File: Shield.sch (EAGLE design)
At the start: 77 parts

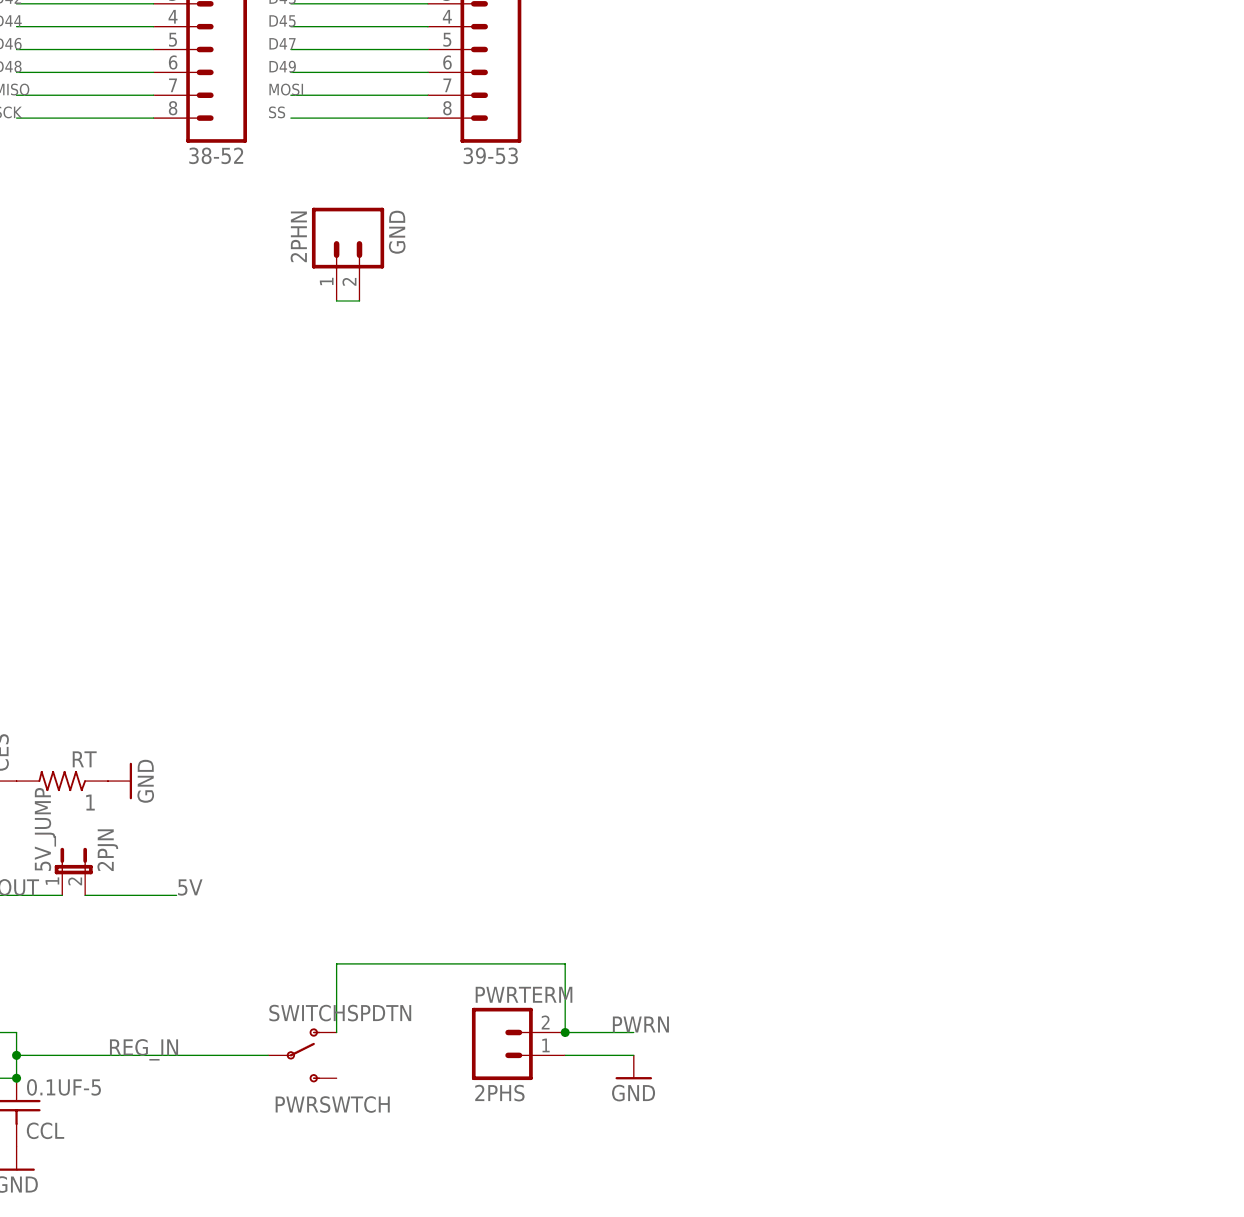
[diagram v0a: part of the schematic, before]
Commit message: Added charging circuit to schematic
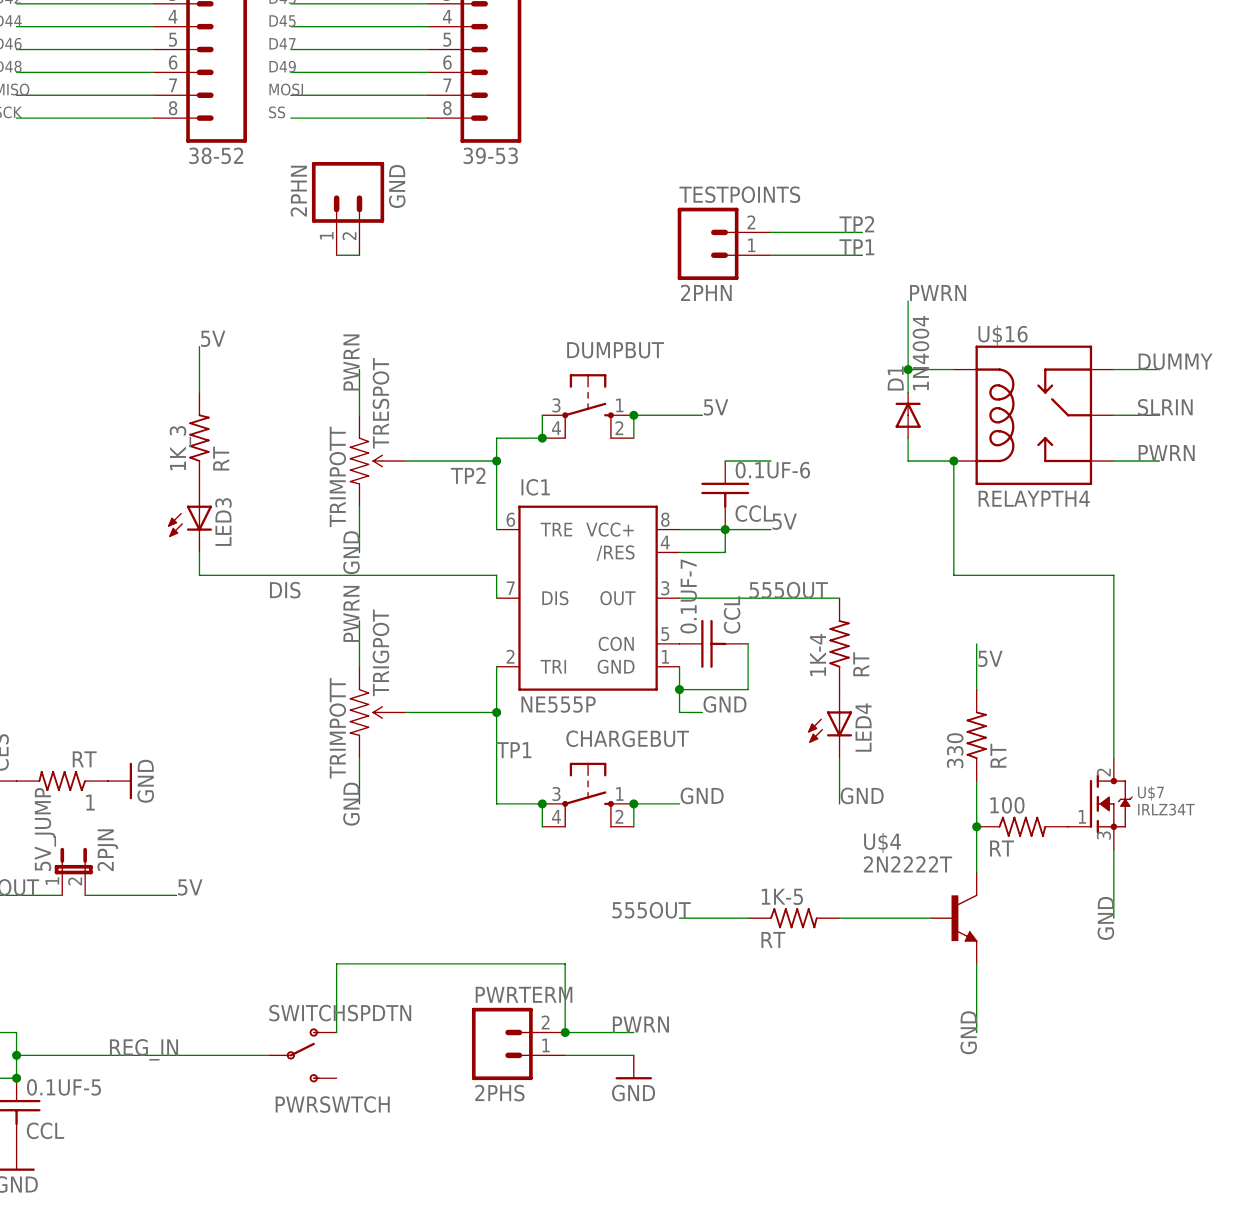
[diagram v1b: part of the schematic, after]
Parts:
- added 0.1UF-6, 0.1UF-7: CCL, LEMS:CCL
- added 100, 1K-4, 1K-5, 1K_3, 330: RT, LEMS:RT
- added CHARGEBUT, DUMPBUT: (no value), LEMS:10-XXN
- added D1: 1N4004, LEMS:1N4004
- added IC1: NE555P, LEMS:NE555P
- added LED3, LED4: (no value), LEMS:LED3MM
- added TESTPOINTS: 2PHN, LEMS:2PHN
- added TRESPOT, TRIGPOT: TRIMPOTT, LEMS:TRIMPOTT
- added U$16: RELAYPTH4, LEMS:RELAYPTH4
- added U$4: 2N2222T, LEMS:2N2222T
- added U$7: IRLZ34T, LEMS:IRLZ34T
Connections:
- new net 555OUT: 1K-4.2, 1K-5.1, IC1.OUT
- new net DIS: IC1.DIS, LED3.C
- new net DUMMY: U$16.NC
- new net N$10: 1K-4.1, LED4.A
- new net N$11: 100.1, 330.1, U$4.C
- new net N$12: 1K-5.2, U$4.B
- new net N$13: 100.2, U$7.G
- new net N$15: D1.A, U$16.COIL2, U$7.D
- new net N$8: 1K_3.1, LED3.A
- new net N$9: 0.1UF-7.1, IC1.CON
- new net SLRIN: U$16.MAIN
- new net TP1: CHARGEBUT.P, CHARGEBUT.P1, IC1.TRI, TESTPOINTS.1, TRIGPOT.WIPER
- new net TP2: DUMPBUT.P, DUMPBUT.P1, IC1.TRE, TESTPOINTS.2, TRESPOT.WIPER
- net 5V: now also 0.1UF-6.2, 1K_3.2, 330.2, DUMPBUT.S, DUMPBUT.S1, IC1./RES, IC1.VCC+
- net GND: now also 0.1UF-6.1, 0.1UF-7.2, CHARGEBUT.S, CHARGEBUT.S1, IC1.GND, LED4.C, TRESPOT.CW, TRIGPOT.CW, U$4.E, U$7.S
- net PWRN: now also D1.C, TRESPOT.CCW, TRIGPOT.CCW, U$16.COIL1, U$16.NO
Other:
- moved on the sheet: GND

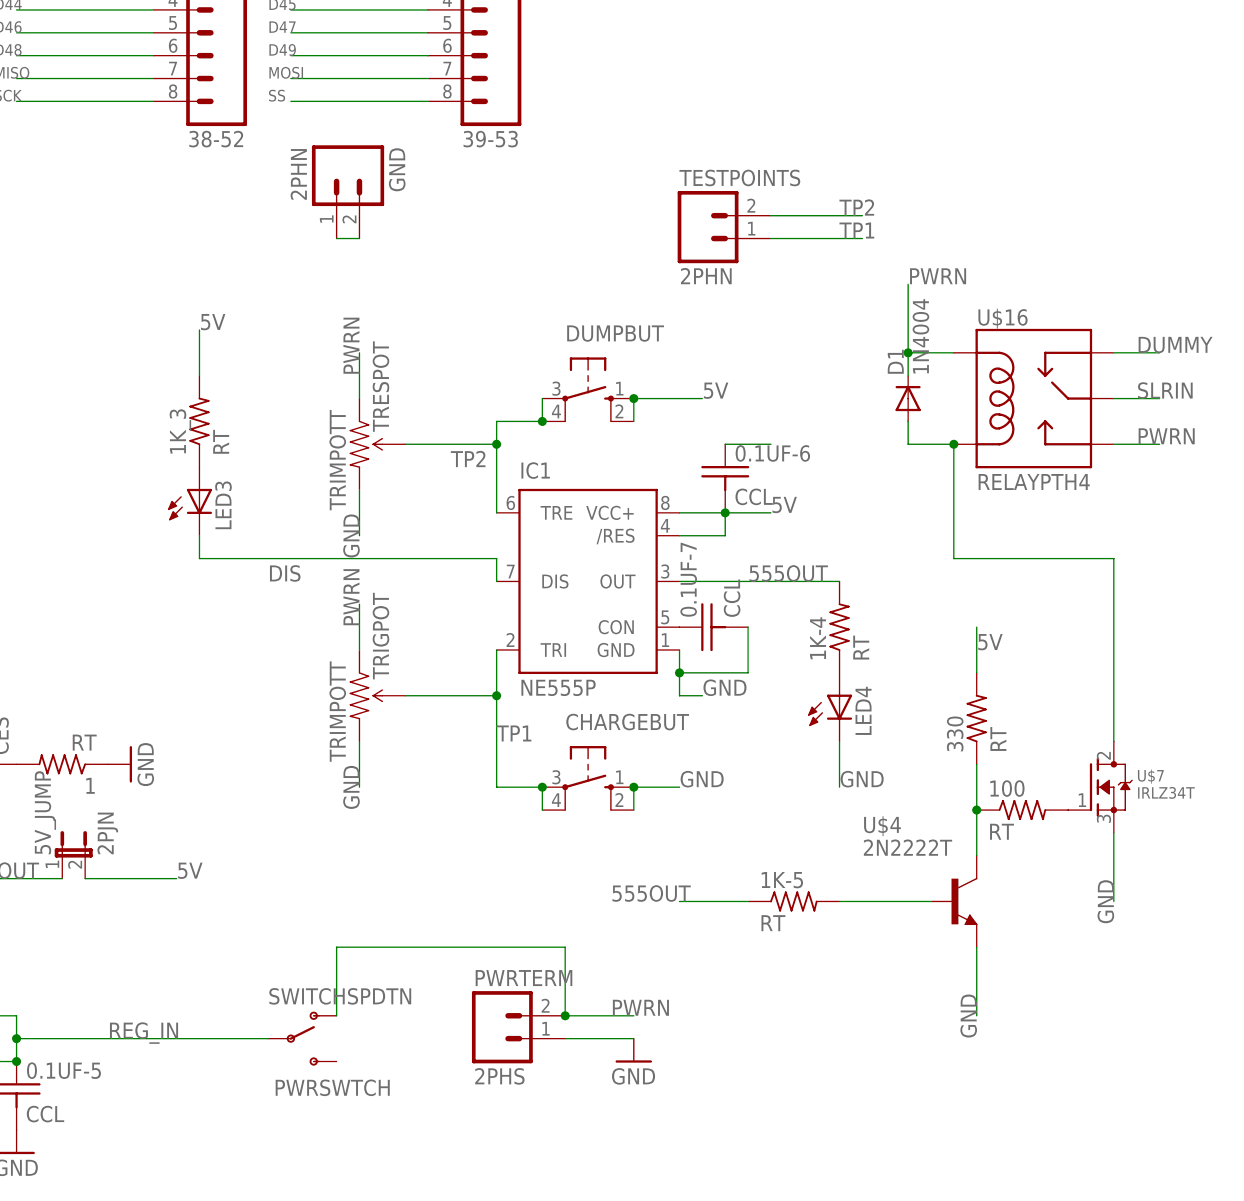
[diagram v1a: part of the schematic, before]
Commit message: Changed charging circuit, finished routing
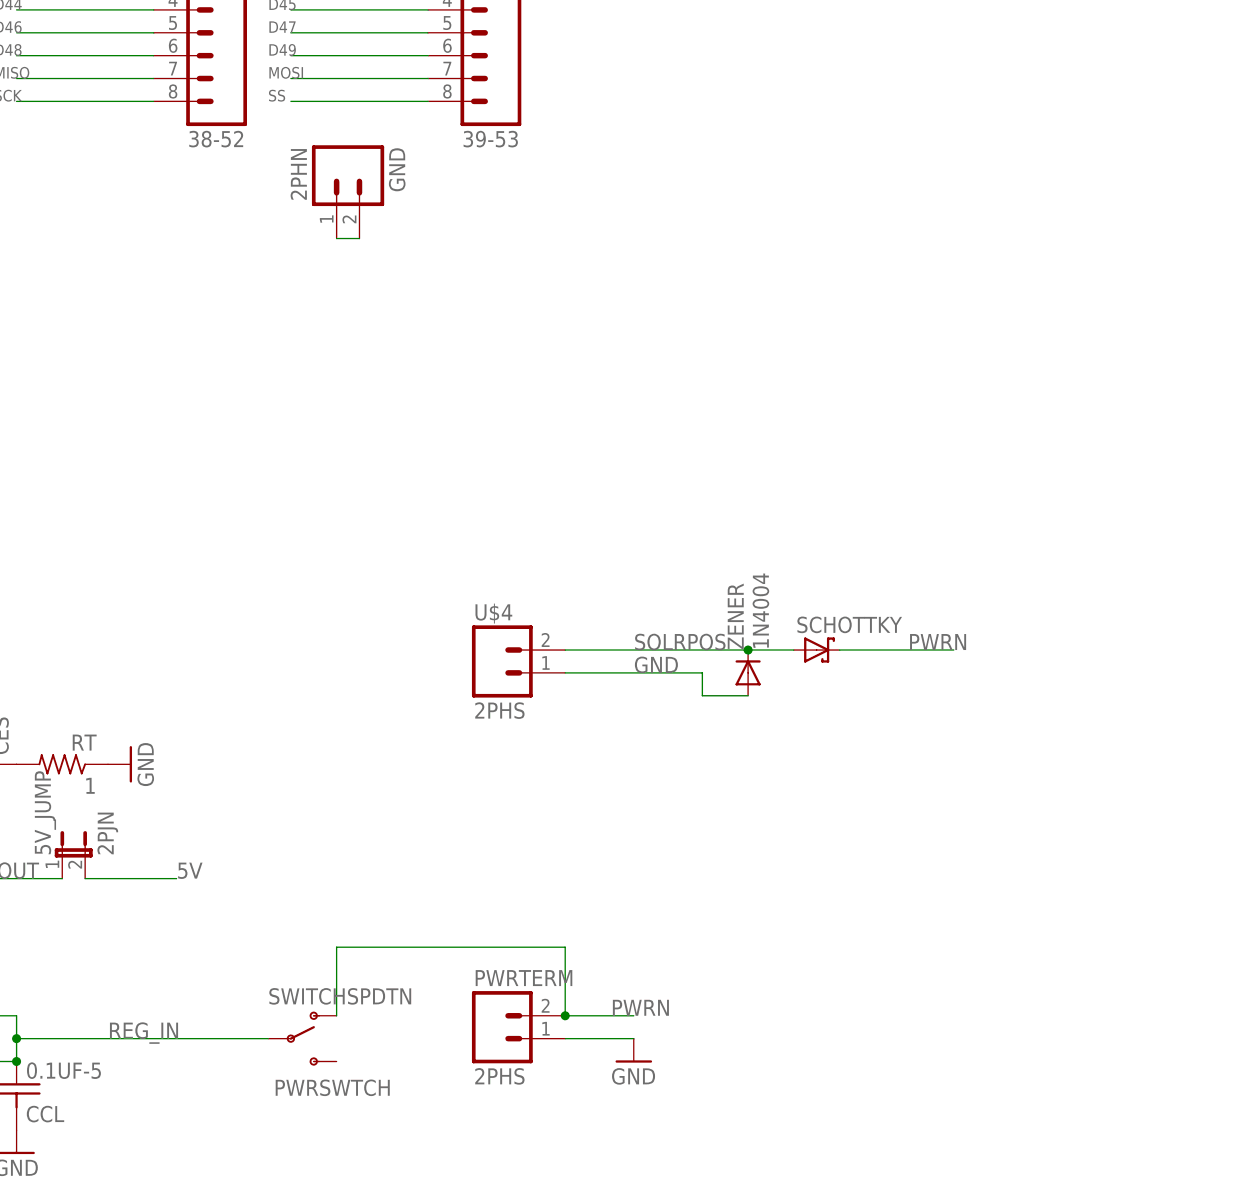
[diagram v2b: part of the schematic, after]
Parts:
- removed 0.1UF-6, 0.1UF-7: CCL, LEMS:CCL
- removed 100, 1K-4, 1K-5, 1K_3, 330: RT, LEMS:RT
- removed CHARGEBUT, DUMPBUT: (no value), LEMS:10-XXN
- removed D1: 1N4004, LEMS:1N4004
- removed IC1: NE555P, LEMS:NE555P
- removed LED3, LED4: (no value), LEMS:LED3MM
- removed TESTPOINTS: 2PHN, LEMS:2PHN
- removed TRESPOT, TRIGPOT: TRIMPOTT, LEMS:TRIMPOTT
- removed U$16: RELAYPTH4, LEMS:RELAYPTH4
- removed U$7: IRLZ34T, LEMS:IRLZ34T
- added SCHOTTKY: (no value), adafruit:SCHOTTKY-DIODEDO41
- added ZENER: 1N4004, LEMS:1N4004
- U$4: value 2N2222T -> 2PHS; device LEMS:2N2222T -> LEMS:2PHS
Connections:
- removed net 555OUT: 1K-4.2, 1K-5.1, IC1.OUT
- removed net DIS: IC1.DIS, LED3.C
- removed net DUMMY: U$16.NC
- removed net N$10: 1K-4.1, LED4.A
- removed net N$11: 100.1, 330.1, U$4.C
- removed net N$12: 1K-5.2, U$4.B
- removed net N$13: 100.2, U$7.G
- removed net N$15: D1.A, U$16.COIL2, U$7.D
- removed net N$8: 1K_3.1, LED3.A
- removed net N$9: 0.1UF-7.1, IC1.CON
- removed net SLRIN: U$16.MAIN
- removed net TP1: CHARGEBUT.P, CHARGEBUT.P1, IC1.TRI, TESTPOINTS.1, TRIGPOT.WIPER
- removed net TP2: DUMPBUT.P, DUMPBUT.P1, IC1.TRE, TESTPOINTS.2, TRESPOT.WIPER
- new net SOLRPOS: SCHOTTKY.A, U$4.2, ZENER.C
- net 5V: no longer 0.1UF-6.2, 1K_3.2, 330.2, DUMPBUT.S, DUMPBUT.S1, IC1./RES, IC1.VCC+
- net GND: now also U$4.1, ZENER.A; no longer 0.1UF-6.1, 0.1UF-7.2, CHARGEBUT.S, CHARGEBUT.S1, IC1.GND, LED4.C, TRESPOT.CW, TRIGPOT.CW, U$4.E, U$7.S
- net PWRN: now also SCHOTTKY.C; no longer D1.C, TRESPOT.CCW, TRIGPOT.CCW, U$16.COIL1, U$16.NO
